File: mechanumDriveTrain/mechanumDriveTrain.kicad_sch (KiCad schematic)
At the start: 0 parts

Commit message: Started working on mechanum drive PCB
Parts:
- added C1: 0.1 uF, Capacitor_SMD:C_0805_2012Metric_Pad1.18x1.45mm_HandSolder, symbol Device:C
- added C2: 560pF, Capacitor_SMD:C_0805_2012Metric_Pad1.18x1.45mm_HandSolder, symbol Device:C
- added IC1: TCAN3414DR, Package_SO:SOIC-8_3.9x4.9mm_P1.27mm, symbol TCAN3414DR:TCAN3414DR
- added J1: XT30U-M, Connector_AMASS:AMASS_XT30U-M_1x02_P5.0mm_Vertical, symbol Connector_Generic:Conn_01x02
- added J2: BM02B-SRSS-TB, Connector_JST:JST_SH_BM02B-SRSS-TB_1x02-1MP_P1.00mm_Vertical, symbol Connector_Generic:Conn_01x02
- added J3, J4: Conn_01x08, Connector_PinSocket_2.54mm:PinSocket_1x08_P2.54mm_Vertical, symbol Connector_Generic:Conn_01x08
- added R1, R2, R3: 60, Resistor_SMD:R_0805_2012Metric_Pad1.20x1.40mm_HandSolder, symbol Device:R_US
- added U1: Teensy 4.1, Custom Footprints:Teensy41, symbol Teensy 4.1:DEV-16771
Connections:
- new net: C2.1, R1.2, R2.1
- new net: U1.3.3V_1 (3.3V), U1.3.3V_2 (3.3V), U1.3.3V_3 (3.3V)
- new net +12V: J1.1 (Pin_1), J4.7 (Pin_7), J4.8 (Pin_8)
- new net +3V3: C1.1, IC1.3 (VCC), J3.7 (Pin_7), R3.2
- new net CANN: IC1.6 (CANL), J2.2 (Pin_2), R2.2
- new net CANP: IC1.7 (CANH), J2.1 (Pin_1), R1.1
- new net C_RX: IC1.4 (RXD), U1.30 (CRX3)
- new net C_TX: IC1.1 (TXD), U1.31 (CTX3)
- new net DIR: J3.2 (Pin_2), U1.1 (TX1)
- new net FLT: J3.5 (Pin_5), R3.1, U1.8 (TX2)
- new net GND: C1.2, C2.2, IC1.2 (GND), IC1.5 (SHDNVIO), IC1.8 (STB), J1.2 (Pin_2), J3.1 (Pin_1), J4.1 (Pin_1), J4.2 (Pin_2), U1.GND1 (GND), U1.GND2 (GND), U1.GND3 (GND), U1.GND4 (GND), U1.GND5 (GND), U1.USB_GND1 (USB_GND), U1.USB_GND2 (USB_GND)
- new net OUTA: J4.3 (Pin_3), J4.4 (Pin_4)
- new net OUTB: J4.5 (Pin_5), J4.6 (Pin_6)
- new net PWM: J3.3 (Pin_3), U1.0 (RX1)
- new net SLP: J3.4 (Pin_4), U1.7 (RX2)
- no-connect marks 0 -> 2
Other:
- note added: "Pololu G2 High-Power Motor Driver 18v17 27.92mm apart"
- note added: "We may need a 5v in i dont think it can take 3V3"
- note added: "for now"
- company: (none) -> Gold Rush Robotics
- title: (none) -> Mechanum Drive Train

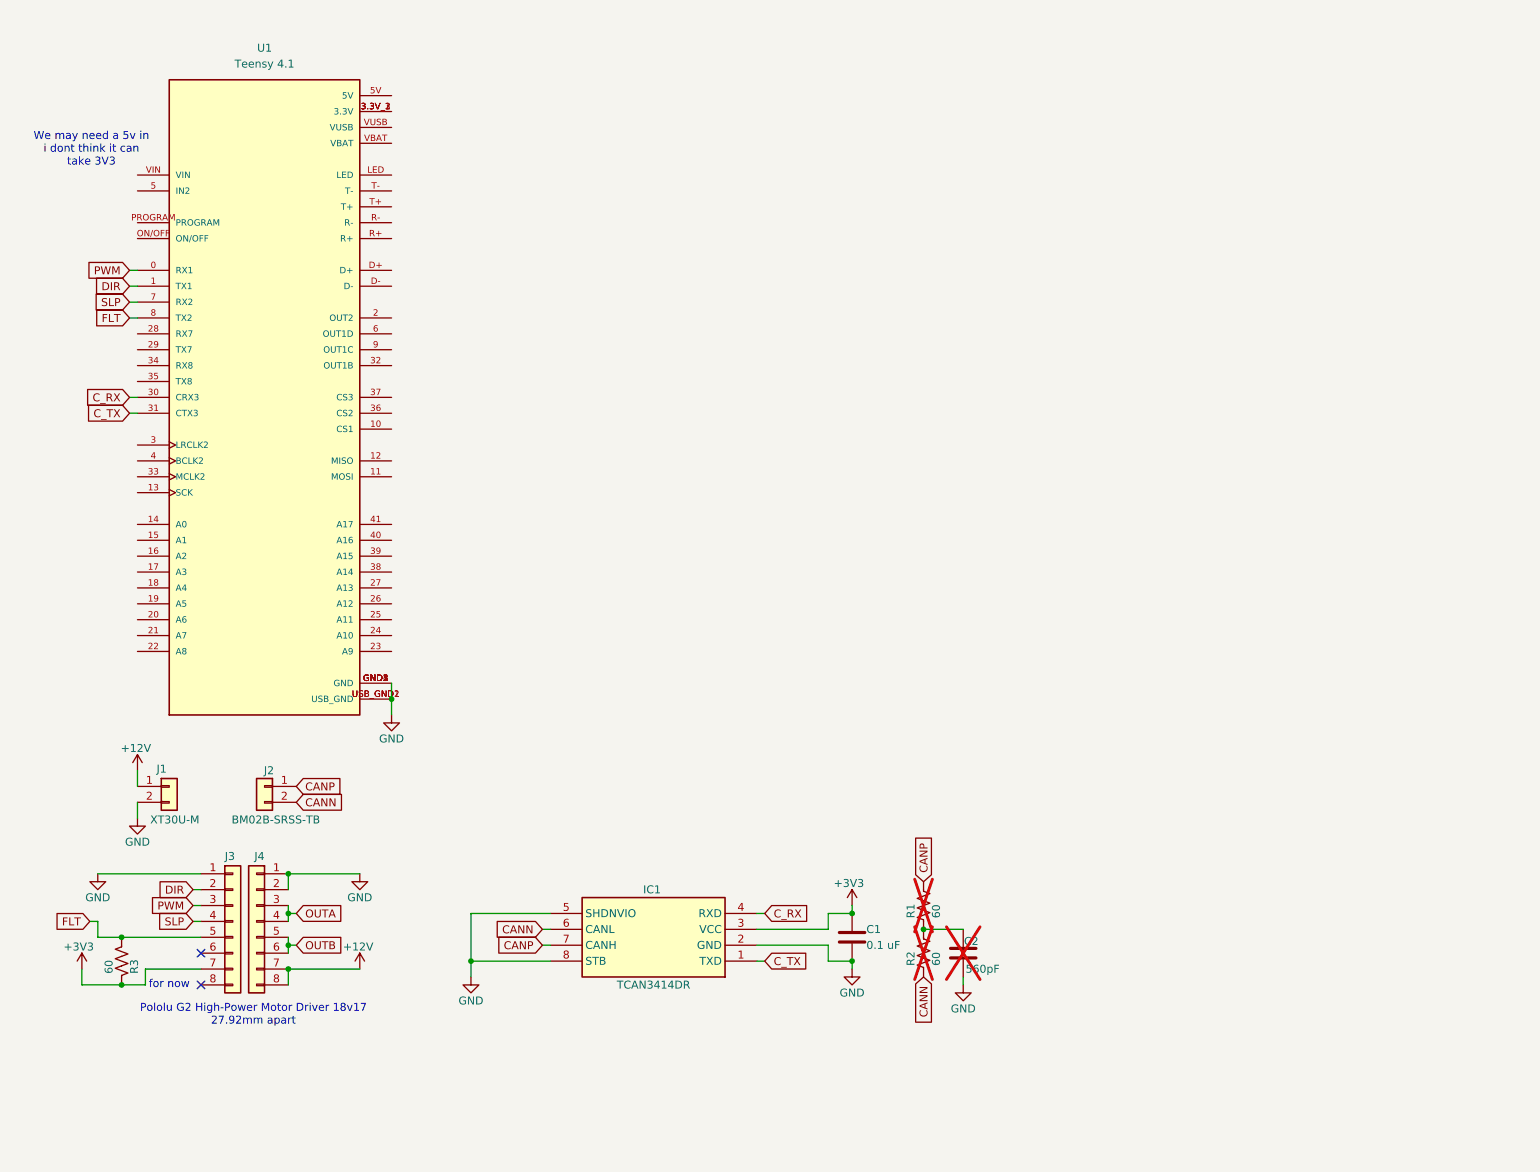
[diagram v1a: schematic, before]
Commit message: Cleaned up schematic, added LDO regulator for 5v to mechanum board
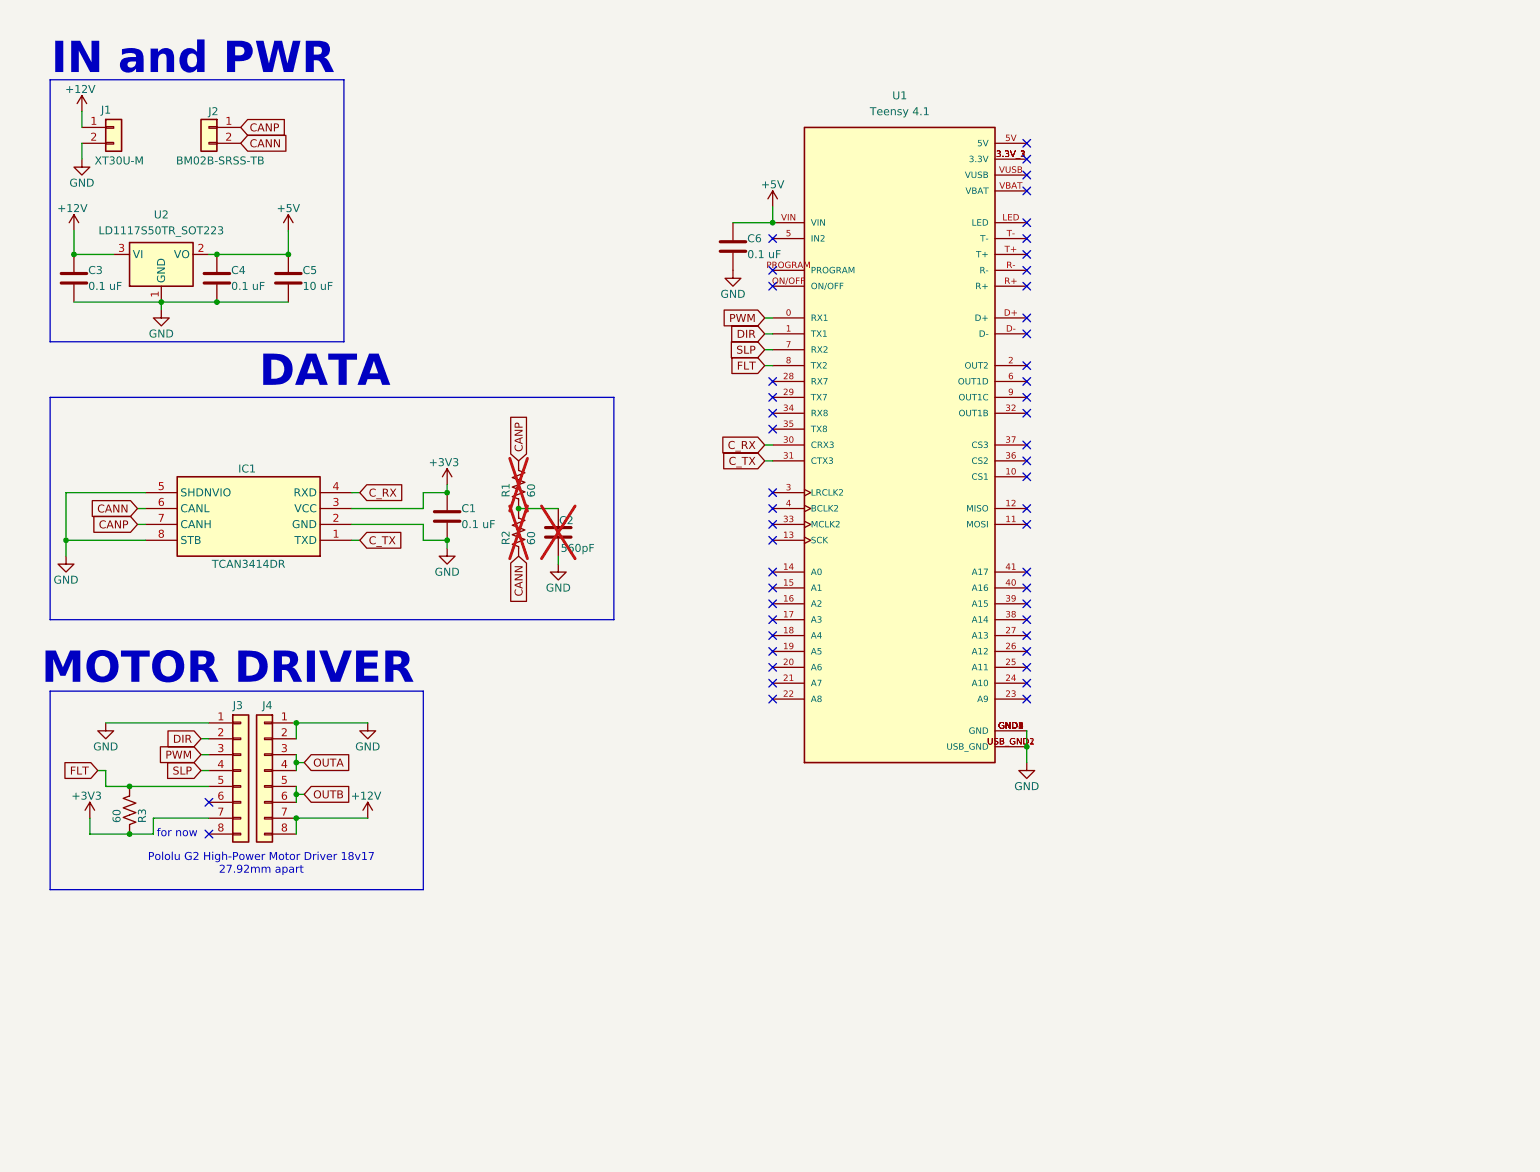
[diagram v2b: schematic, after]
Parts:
- added C3, C4, C6: 0.1 uF, Capacitor_SMD:C_0805_2012Metric_Pad1.18x1.45mm_HandSolder, symbol Device:C
- added C5: 10 uF, Capacitor_SMD:C_0805_2012Metric_Pad1.18x1.45mm_HandSolder, symbol Device:C
- added U2: LD1117S50TR_SOT223, Package_TO_SOT_SMD:SOT-223-3_TabPin2, symbol Regulator_Linear:LD1117S50TR_SOT223
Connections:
- net +12V: now also C3.1, U2.3 (VI)
- net GND: now also C3.2, C4.2, C5.2, C6.2, U2.1 (GND)
- net +5V: now reaches U1.VIN
- net +5V: now also C4.1, C5.1, C6.1, U2.2 (VO)
- no-connect marks 2 -> 51
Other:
- note added: "DATA"
- note added: "IN and PWR"
- note added: "MOTOR DRIVER"
- note removed: "We may need a 5v in i dont think it can take 3V3"
- moved on the sheet: C1, C2, IC1, J1, J2, J3, J4, R1, R2, R3, U1

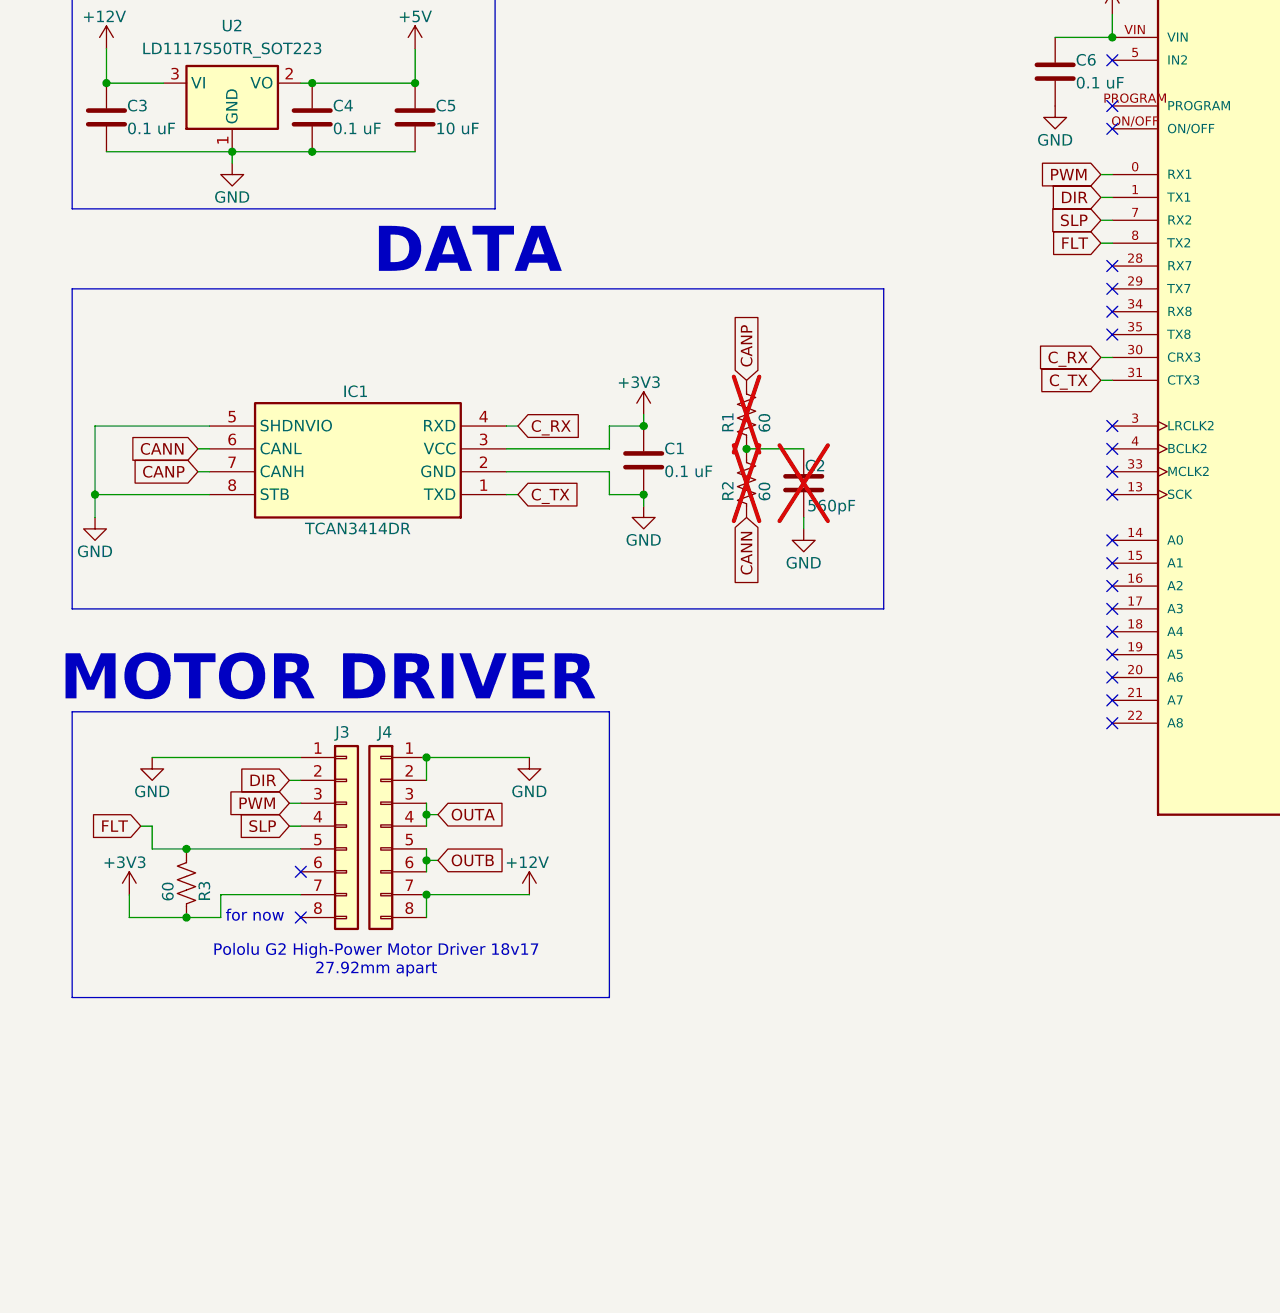
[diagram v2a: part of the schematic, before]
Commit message: Added a 2nd pololu board
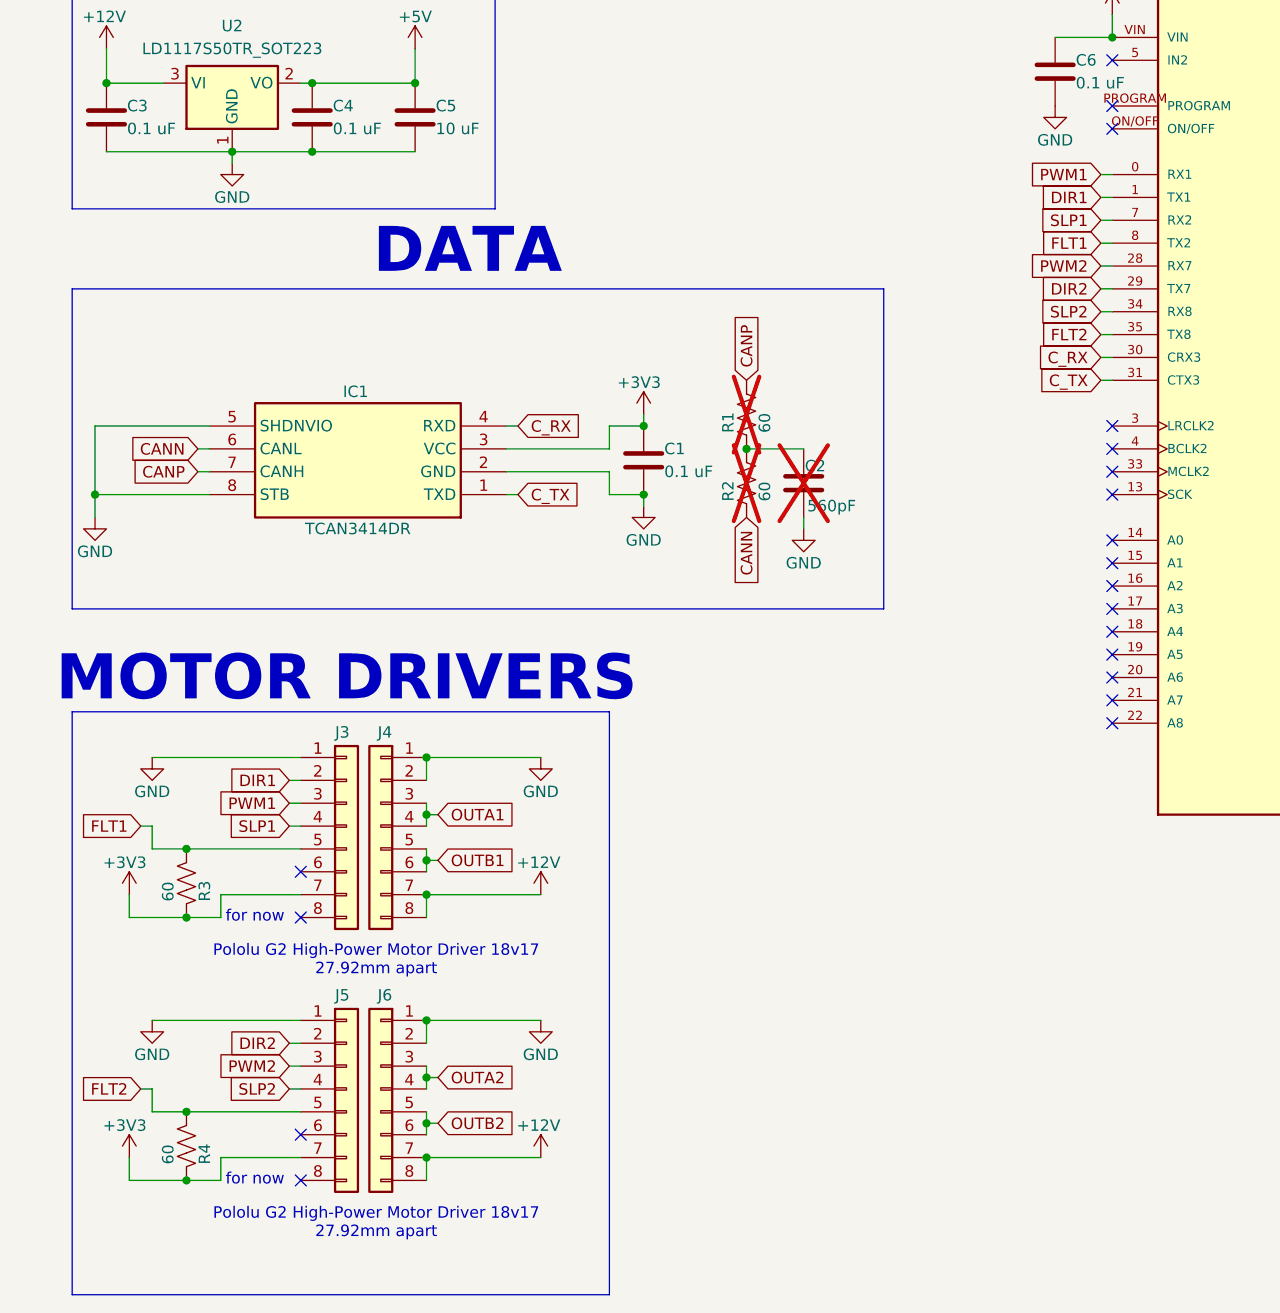
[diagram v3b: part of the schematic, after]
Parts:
- added J5, J6: Conn_01x08, Connector_PinSocket_2.54mm:PinSocket_1x08_P2.54mm_Vertical, symbol Connector_Generic:Conn_01x08
- added R4: 60, Resistor_SMD:R_0805_2012Metric_Pad1.20x1.40mm_HandSolder, symbol Device:R_US
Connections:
- net +12V: now also J6.7 (Pin_7), J6.8 (Pin_8)
- net +3V3: now also J5.7 (Pin_7), R4.2
- net GND: now also J5.1 (Pin_1), J6.1 (Pin_1), J6.2 (Pin_2)
- net PWM2: now reaches U1.28 (RX7)
- net PWM2: now also J5.3 (Pin_3)
- net DIR2: now reaches U1.29 (TX7)
- net DIR2: now also J5.2 (Pin_2)
- net SLP2: now reaches U1.34 (RX8)
- net SLP2: now also J5.4 (Pin_4)
- net FLT2: now reaches U1.35 (TX8)
- net FLT2: now also J5.5 (Pin_5), R4.1
- net DIR renamed DIR1
- net FLT renamed FLT1
- net OUTA renamed OUTA1
- net OUTB renamed OUTB1
- net PWM renamed PWM1
- net SLP renamed SLP1
- new net OUTA2: J6.3 (Pin_3), J6.4 (Pin_4)
- new net OUTB2: J6.5 (Pin_5), J6.6 (Pin_6)
- no-connect marks 51 -> 49
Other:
- note added: "MOTOR DRIVERS"
- note removed: "MOTOR DRIVER"
